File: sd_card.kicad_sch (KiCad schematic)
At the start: 6 parts, among them J15 MicroSD_693071020811, U46 ESD204DQAR, U47 ESD204DQAR

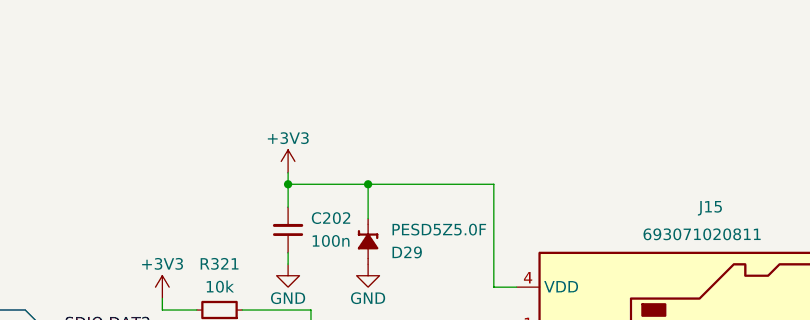
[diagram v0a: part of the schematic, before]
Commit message: [#70030] Unify functional block names
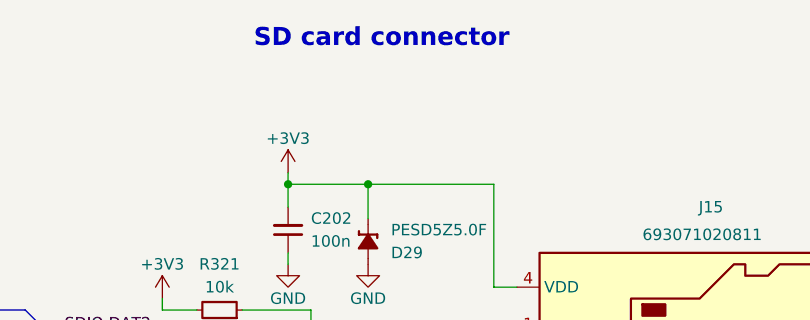
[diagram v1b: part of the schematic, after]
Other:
- note added: "SD card connector"
- company: Antmicro Ltd. -> Antmicro Ltd
- title: Com Express 7 baseboard -> COM Express 7 Baseboard
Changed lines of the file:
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@@
 	(paper "A3")
 	(title_block
-		(title "Com Express 7 baseboard")
-		(date "2024-03-28")
+		(title "COM Express 7 Baseboard")
+		(date "2024-12-13")
 		(rev "1.1.0")
-		(company "Antmicro Ltd.")
+		(company "Antmicro Ltd")
+		(comment 1 "www.antmicro.com")
 	)
 	(bus_alias "SDIO"
@@
 		)
 	)
+	(text "SD card connector"
+		(exclude_from_sim no)
+		(at 209.55 110.744 0)
+		(effects
+			(font
+				(size 2 2)
+				(thickness 0.8)
+				(bold yes)
+			)
+			(justify left bottom)
+		)
+	)
